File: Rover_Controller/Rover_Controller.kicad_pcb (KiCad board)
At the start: 2 copper layers, 137.6 x 81.5 mm, 36 parts, among them Q1 S8050, SW1 SW_SPST, SW2 SW_SPST, SW3 SW_SPST, SW4 SW_SPST

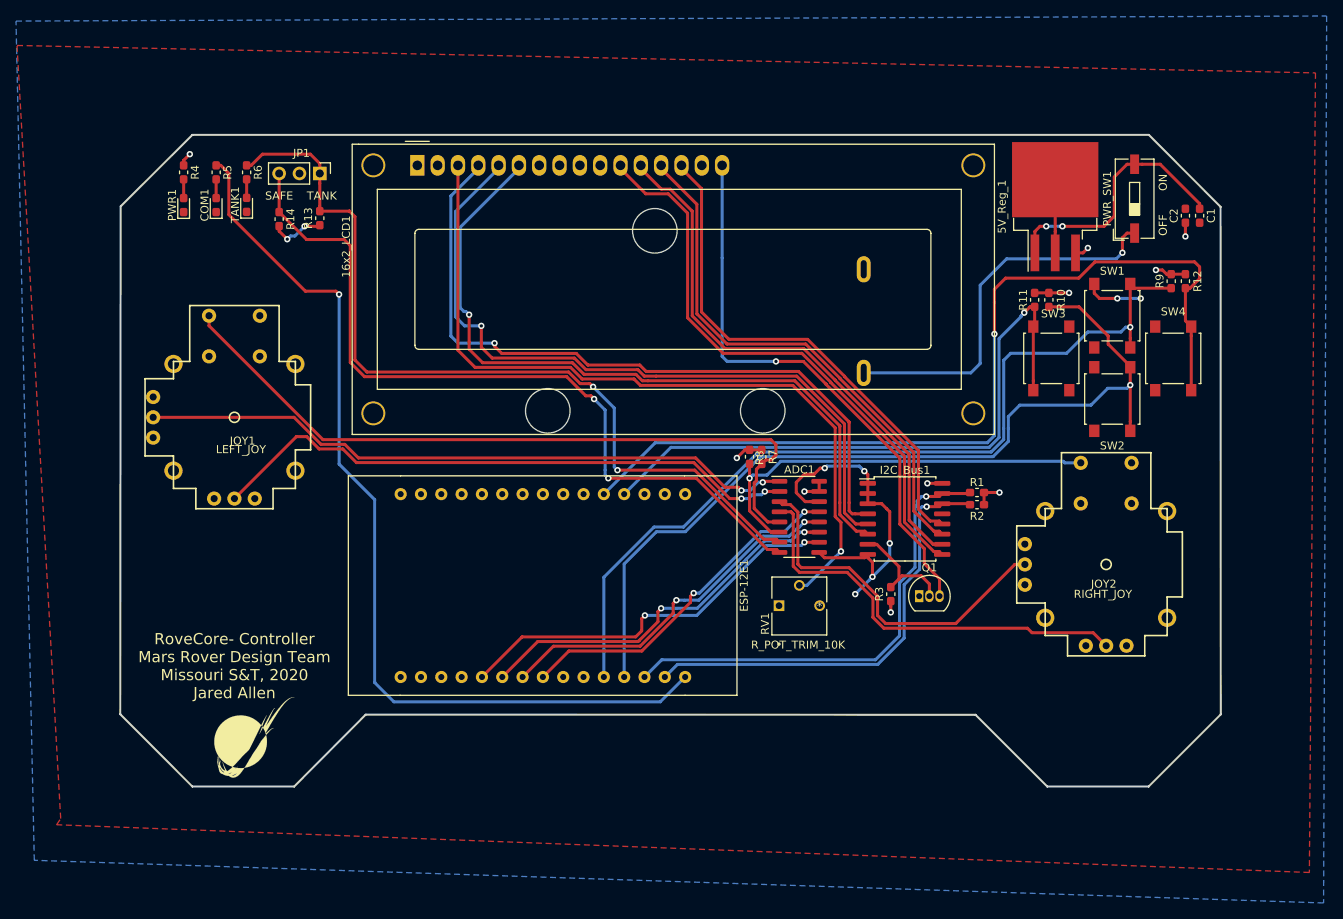
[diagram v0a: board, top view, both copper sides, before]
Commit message: Button Footprints Updated
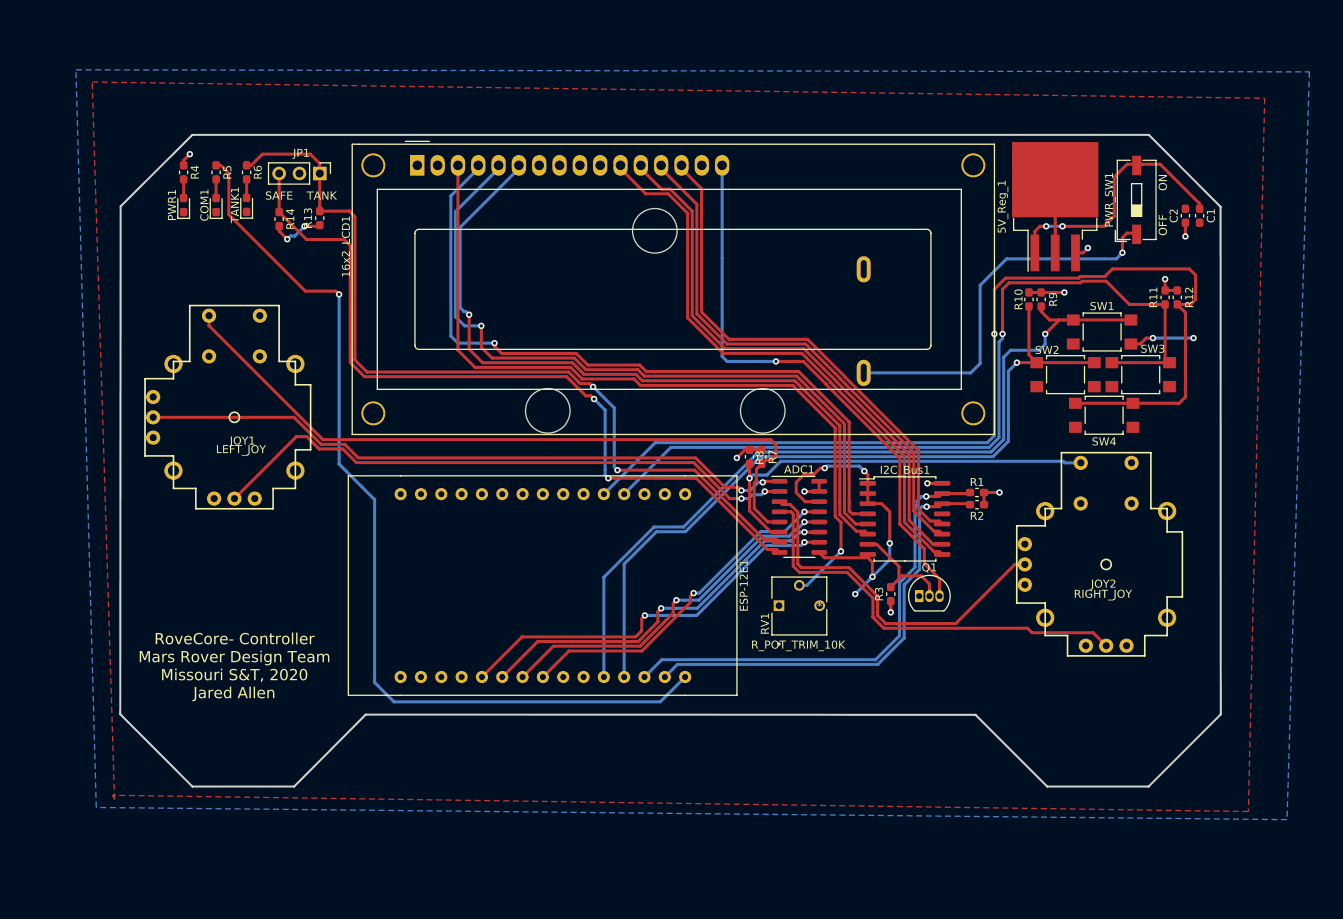
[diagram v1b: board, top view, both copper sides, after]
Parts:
- removed G***: LOGO, MRDT_Silkscreens:0_MRDT_Logo_10mm
- SW1, SW2, SW3, SW4: value SW_SPST -> SW_Push; footprint Button_Switch_SMD:SW_SPST_B3S-1000 -> Button_Switch_SMD:SW_SPST_TL3305A
- moved R9 16.4 mm to (191.0, 72.6)
- moved R11 16.3 mm to (206.5, 72.4)
- moved SW3 11.4 mm to (203.5, 82.0), turned to 0 degrees
- moved SW4 11.2 mm to (198.9, 87.1), turned to 0 degrees
- moved SW2 6.59 mm to (194.1, 82.0), turned to 0 degrees
- moved R10 2.49 mm to (189.5, 72.6)
- moved SW1 2.40 mm to (198.6, 76.7), turned to 0 degrees
- moved R12 2.27 mm to (208.0, 72.4)
- moved PWR_SW1 0.30 mm to (202.9, 60.2)
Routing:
- net SW3: track 78.8 -> 105.1 mm
- net SW2: track 110.4 -> 96.0 mm
- net SW4: track 114.3 -> 128.3 mm
- net SW1: track 110.3 -> 101.8 mm
- net GND: track 68.3 -> 69.2 mm
- net 5V: track 26.8 -> 26.0 mm

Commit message: 5V PCB Trace Pads Updated
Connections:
- net 5V renamed +5V

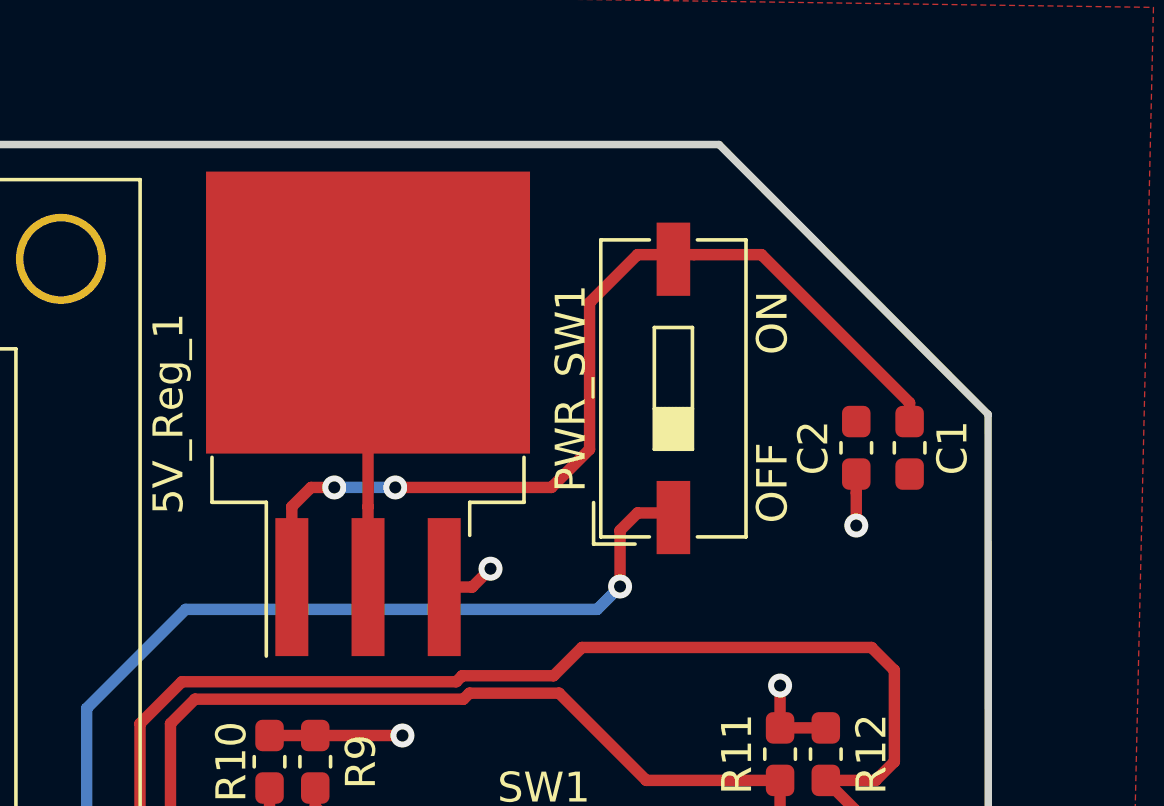
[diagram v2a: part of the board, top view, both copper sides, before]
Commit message: Slide Switch Changed to Angled Switch
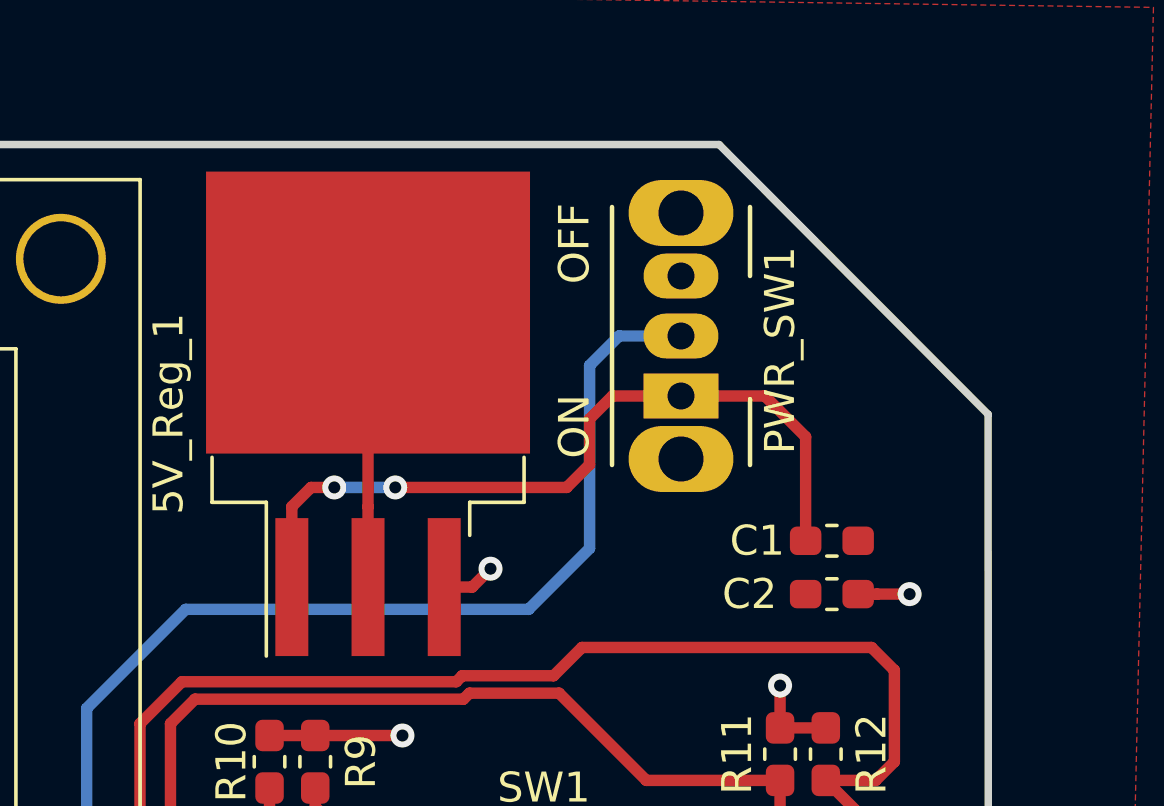
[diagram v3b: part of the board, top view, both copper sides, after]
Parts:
- PWR_SW1: value SW_SPST -> SW_SPDT; footprint Button_Switch_SMD:SW_DIP_SPSTx01_Slide_9.78x4.72mm_W8.61mm_P2.54mm -> Button_Switch_THT:SW_CuK_OS102011MA1QN1_SPDT_Angled
- moved C2 4.94 mm to (208.2, 67.1), turned to 180 degrees
- moved C1 4.04 mm to (208.2, 65.3), turned to 0 degrees
- moved PWR_SW1 0.36 mm to (203.2, 60.5)
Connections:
- PWR_SW1 pad 1: Net-(BT1-Pad1) -> Net-(5V_Reg_1-Pad1)
- PWR_SW1 pad 2: Net-(5V_Reg_1-Pad1) -> Net-(BT1-Pad1)
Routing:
- net Net-(5V_Reg_1-Pad1): track 32.3 -> 26.3 mm
- net Net-(BT1-Pad1): track 47.9 -> 53.4 mm, vias 1 -> 0

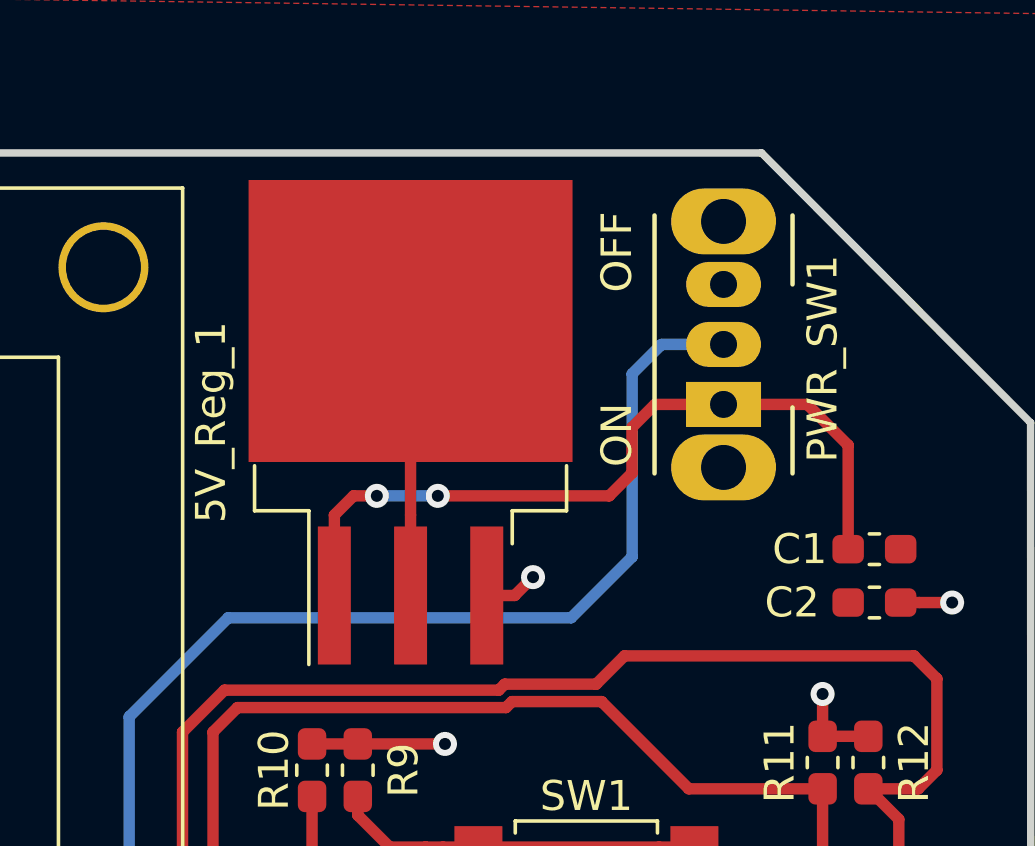
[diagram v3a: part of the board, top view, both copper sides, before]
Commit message: 7805 Package Updated
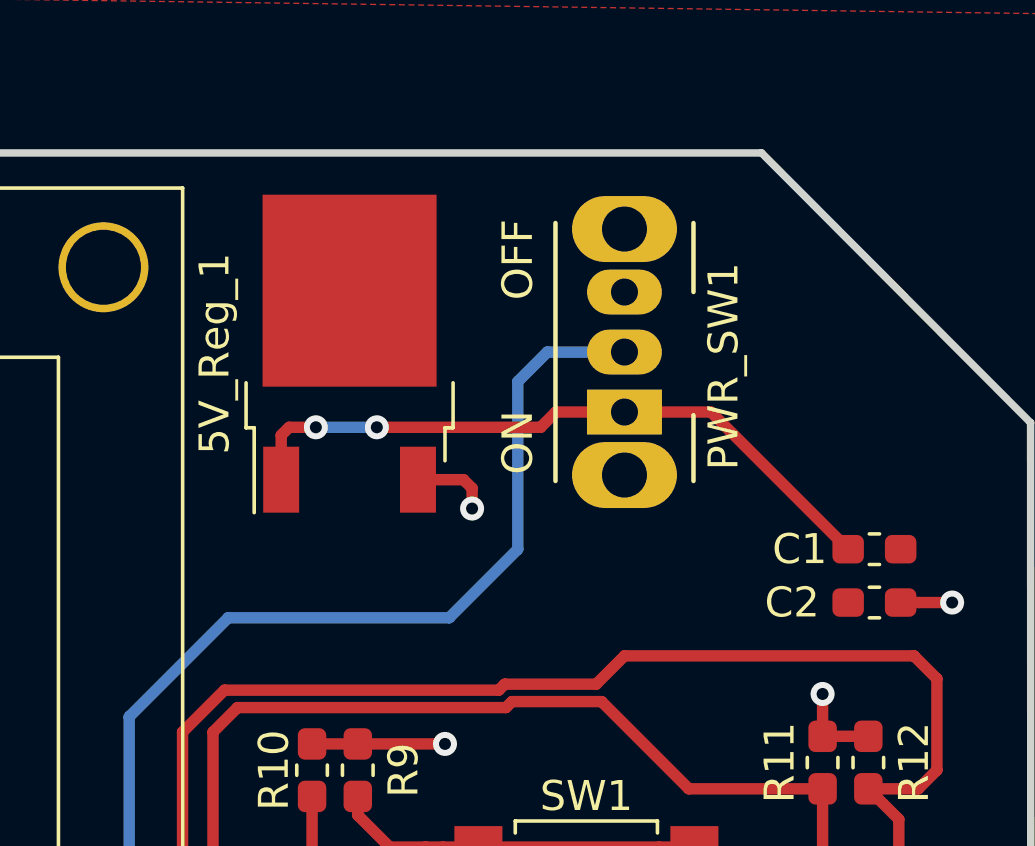
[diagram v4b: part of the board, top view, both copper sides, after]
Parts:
- 5V_Reg_1: footprint Package_TO_SOT_SMD:TO-263-3_TabPin2 -> Package_TO_SOT_SMD:TO-252-2
- moved PWR_SW1 3.31 mm to (199.9, 60.7)
- moved 5V_Reg_1 3.06 mm to (190.7, 58.8)
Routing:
- net GND: track 69.2 -> 58.3 mm
- net Net-(BT1-Pad1): track 53.4 -> 49.6 mm
- net Net-(5V_Reg_1-Pad1): track 26.3 -> 22.6 mm
- net +5V: track 26.0 -> 26.8 mm

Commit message: BOM and Signature Updated
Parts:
- added G***: LOGO, MRDT_Silkscreens:z_sig_Jared_Allen, F.Cu at (94.2, 127.3)
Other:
- board text added: "PR Controller Rev. 1 Mars Rover Design Team Missouri S&T, 2020 Jared Allen"
- board text removed: "RoveCore- Controller Mars Rover Design Team Missouri S&T, 2020 Jared Allen"

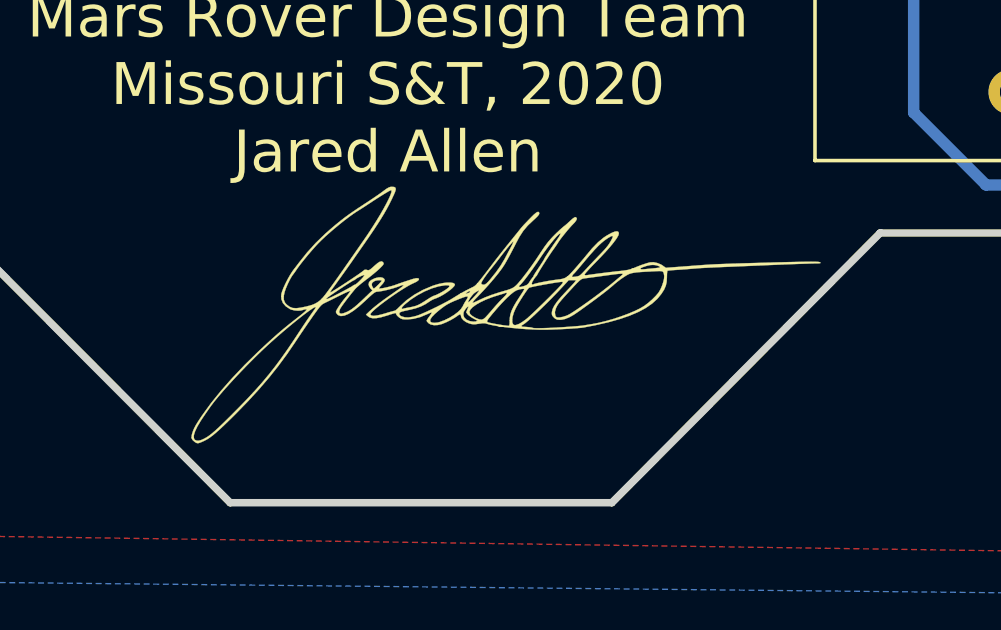
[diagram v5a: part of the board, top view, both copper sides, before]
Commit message: Signature File Location Changed
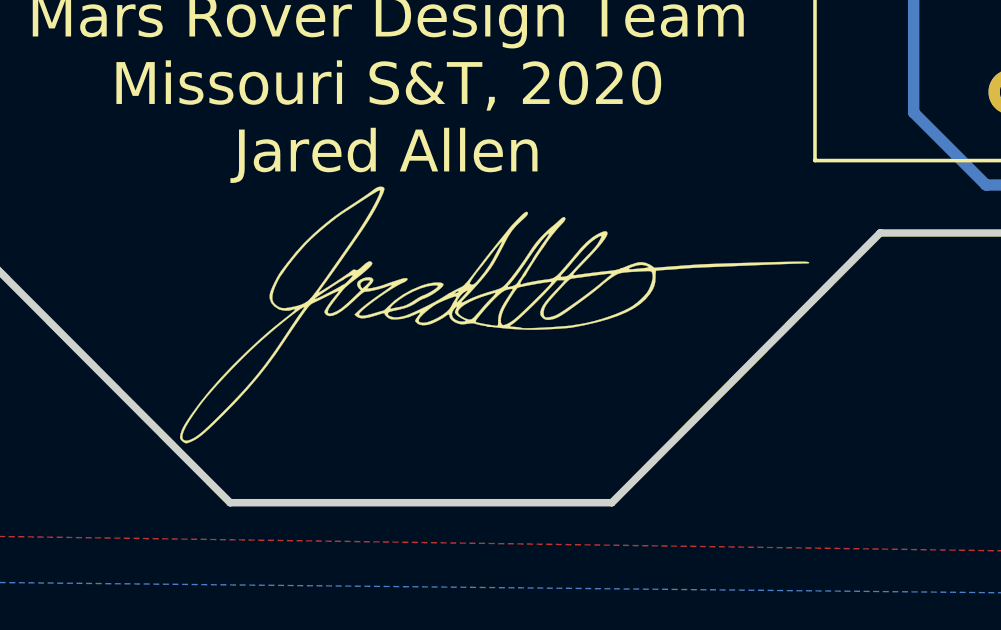
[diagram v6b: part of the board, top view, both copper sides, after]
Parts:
- removed the G*** at (94.2, 127.3)
- added G***: LOGO, Rover_Controller:z_sig_Jared_Allen, F.Cu at (93.9, 127.3)
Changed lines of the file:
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@@
     (add_net k)
   )
-  (module MRDT_Silkscreens:z_sig_Jared_Allen (layer F.Cu)
-    (at 94.234 127.254)
+  (module Rover_Controller:z_sig_Jared_Allen (layer F.Cu)
+    (at 93.853 127.254)
     (fp_text reference G*** (at 0 0) (layer F.SilkS) hide
       (effects (font (size 1.524 1.524) (thickness 0.3)))
